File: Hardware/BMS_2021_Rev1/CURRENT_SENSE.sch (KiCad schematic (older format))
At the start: 5 parts

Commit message: cell filter mods, changing current sense circuit, 3v3/5v worked on
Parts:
- removed R?: R_Shunt, symbol Device:R_Shunt
- added R? (x3): 5mΩ, symbol Device:R
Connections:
- wire segments 38 -> 39
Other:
- note removed: "Doucmentation says connect VBUS to power supply rail, does this work\n"
- note removed: "Where should PV and ground go?\n"
- moved on the sheet: C?, R?

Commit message: changed current sense circuit to op amp
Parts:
- removed C?: C, symbol Device:C
- removed R? (x2): R, symbol Device:R
- removed U?: INA226, Package_SO:VSSOP-10_3x3mm_P0.5mm, symbol Analog_ADC:INA226
- added Q?: Q_NMOS_DGS, symbol Device:Q_NMOS_DGS
- added R? (x2): 27Ω, symbol Device:R
- added R?: 300Ω, symbol Device:R
- added U?: OPAMP, symbol pspice:OPAMP
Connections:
- net labels removed: +5V, I2C_Interface(?)
- wire segments 39 -> 24
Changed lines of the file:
@@
 	1950 850  2050 850
-Wire Wire Line
-	1550 1100 1550 850
 Wire Wire Line
 	1550 850  1650 850
@@
 	0    1    1    0
 $EndComp
-Connection ~ 6450 2900
+$Comp
+L pspice:OPAMP U?
+U 1 1 5F835DEC
+P 2200 1700
+F 0 "U?" V 2154 2044 50  0000 L CNN
+F 1 "OPAMP" V 2245 2044 50  0000 L CNN
+F 2 "" H 2200 1700 50  0001 C CNN
+F 3 "~" H 2200 1700 50  0001 C CNN
+	1    2200 1700
+	0    1    1    0
+$EndComp
+$Comp
+L Device:R R?
+U 1 1 5F8362F1
+P 1850 1150
+F 0 "R?" V 1760 1150 50  0000 C CNN
+F 1 "27Ω" V 1850 1150 39  0000 C CNN
+F 2 "" V 1780 1150 50  0001 C CNN
+F 3 "~" H 1850 1150 50  0001 C CNN
+	1    1850 1150
+	0    1    1    0
+$EndComp
+$Comp
+L Device:R R?
+U 1 1 5F83721F
+P 2550 1150
+F 0 "R?" V 2460 1150 50  0000 C CNN
+F 1 "27Ω" V 2550 1150 39  0000 C CNN
+F 2 "" V 2480 1150 50  0001 C CNN
+F 3 "~" H 2550 1150 50  0001 C CNN
+	1    2550 1150
+	0    1    1    0
+$EndComp
 Wire Wire Line
-	6450 3050 6450 2900
+	2700 1150 2850 1150
 Wire Wire Line
-	7100 1650 7100 3050
-Text GLabel 6650 2350 3    50   Output ~ 0
-I2C_Interface(?)
-Text GLabel 6200 2350 0    50   Output ~ 0
-I2C_Interface(?)
+	1550 1150 1700 1150
+Wire Wire Line
+	1550 850  1550 1150
+Wire Wire Line
+	2000 1150 2100 1150
+Wire Wire Line
+	2300 1150 2400 1150
+Wire Wire Line
+	1900 1600 1800 1600
+Wire Wire Line
+	1800 1600 1800 1650
+Wire Wire Line
+	2500 1600 2700 1600
+Text HLabel 2700 1600 2    50   Input ~ 0
+PV
 $Comp
 L power:GND #PWR?
-U 1 1 5F7FBB9B
-P 7200 2050
-AR Path="/5F80E1AD/5F7FBB9B" Ref="#PWR?"  Part="1"
-AR Path="/5F80341F/5F7FBB9B" Ref="#PWR?"  Part="1"
-F 0 "#PWR?" H 7200 1800 50  0001 C CNN
-F 1 "GND" H 7205 1877 50  0000 C CNN
-F 2 "" H 7200 2050 50  0001 C CNN
-F 3 "" H 7200 2050 50  0001 C CNN
-	1    7200 2050
-	1    0    0    -1
-$EndComp
-$Comp
-L Device:C C?
-U 1 1 5F7FB581
-P 7200 1900
-AR Path="/5F80E1AD/5F7FB581" Ref="C?"  Part="1"
-AR Path="/5F80341F/5F7FB581" Ref="C?"  Part="1"
-F 0 "C?" H 7315 1946 50  0000 L CNN
-F 1 "C" H 7315 1855 50  0000 L CNN
-F 2 "" H 7238 1750 50  0001 C CNN
-F 3 "~" H 7200 1900 50  0001 C CNN
-	1    7200 1900
+U 1 1 5F83E3C7
+P 1800 1650
+F 0 "#PWR?" H 1800 1400 50  0001 C CNN
+F 1 "GND" H 1805 1477 50  0000 C CNN
+F 2 "" H 1800 1650 50  0001 C CNN
+F 3 "" H 1800 1650 50  0001 C CNN
+	1    1800 1650
 	1    0    0    -1
 $EndComp
 Wire Wire Line
-	7100 1650 7100 1550
-Connection ~ 7100 1650
+	2850 850  2850 1150
 Wire Wire Line
-	7200 1650 7200 1750
+	2100 1150 2100 1300
 Wire Wire Line
-	7100 1650 7200 1650
-Connection ~ 7100 1550
+	2300 1150 2300 1400
+Connection ~ 2100 1300
 Wire Wire Line
-	6450 3050 7100 3050
+	2100 1300 2100 1400
 Wire Wire Line
-	6450 2900 6450 2750
+	1550 1300 1550 2300
 Wire Wire Line
-	6300 2900 6450 2900
-Wire Wire Line
-	6300 2750 6300 2900
-Wire Wire Line
-	6500 2300 6500 2400
-Connection ~ 6500 2300
-Wire Wire Line
-	6650 2300 6650 2350
-Wire Wire Line
-	6500 2300 6650 2300
-Wire Wire Line
-	6300 2350 6300 2450
-Connection ~ 6300 2350
-Wire Wire Line
-	6300 2350 6200 2350
-Wire Wire Line
-	6400 1950 6400 2150
-Wire Wire Line
-	6300 2150 6300 2350
-Wire Wire Line
-	6400 2150 6300 2150
-Wire Wire Line
-	6450 2400 6450 2450
-Wire Wire Line
-	6500 2400 6450 2400
-Wire Wire Line
-	6500 1950 6500 2300
+	1550 1300 2100 1300
 $Comp
-L Device:R R?
-U 1 1 5F7F7183
-P 6450 2600
-AR Path="/5F80E1AD/5F7F7183" Ref="R?"  Part="1"
-AR Path="/5F80341F/5F7F7183" Ref="R?"  Part="1"
-F 0 "R?" H 6520 2646 50  0000 L CNN
-F 1 "R" H 6520 2555 50  0000 L CNN
-F 2 "" V 6380 2600 50  0001 C CNN
-F 3 "~" H 6450 2600 50  0001 C CNN
-	1    6450 2600
-	1    0    0    -1
-$EndComp
-$Comp
-L Device:R R?
-U 1 1 5F7F6224
-P 6300 2600
-AR Path="/5F80E1AD/5F7F6224" Ref="R?"  Part="1"
-AR Path="/5F80341F/5F7F6224" Ref="R?"  Part="1"
-F 0 "R?" H 6150 2650 50  0000 L CNN
-F 1 "R" H 6150 2550 50  0000 L CNN
-F 2 "" V 6230 2600 50  0001 C CNN
-F 3 "~" H 6300 2600 50  0001 C CNN
-	1    6300 2600
+L Device:Q_NMOS_DGS Q?
+U 1 1 5F852FE1
+P 2100 2300
+F 0 "Q?" H 2304 2346 50  0000 L CNN
+F 1 "Q_NMOS_DGS" H 2304 2255 50  0000 L CNN
+F 2 "" H 2300 2400 50  0001 C CNN
+F 3 "~" H 2100 2300 50  0001 C CNN
+	1    2100 2300
 	1    0    0    -1
 $EndComp
 Wire Wire Line
-	6800 1150 6800 1000
+	2200 2000 2200 2100
+Wire Wire Line
+	1550 2300 1900 2300
+Wire Wire Line
+	2200 2500 2200 2750
+$Comp
+L Device:R R?
+U 1 1 5F85658D
+P 2200 2900
+F 0 "R?" H 2130 2900 50  0000 R CNN
+F 1 "300Ω" V 2200 2980 39  0000 R CNN
+F 2 "" V 2130 2900 50  0001 C CNN
+F 3 "~" H 2200 2900 50  0001 C CNN
+	1    2200 2900
+	-1   0    0    1
+$EndComp
+Wire Wire Line
+	2200 3050 2200 3150
 $Comp
 L power:GND #PWR?
-U 1 1 5F7F4F0A
-P 6800 2150
-AR Path="/5F80E1AD/5F7F4F0A" Ref="#PWR?"  Part="1"
-AR Path="/5F80341F/5F7F4F0A" Ref="#PWR?"  Part="1"
-F 0 "#PWR?" H 6800 1900 50  0001 C CNN
-F 1 "GND" H 6805 1977 50  0000 C CNN
-F 2 "" H 6800 2150 50  0001 C CNN
-F 3 "" H 6800 2150 50  0001 C CNN
-	1    6800 2150
+U 1 1 5F859B0F
+P 2200 3150
+F 0 "#PWR?" H 2200 2900 50  0001 C CNN
+F 1 "GND" H 2205 2977 50  0000 C CNN
+F 2 "" H 2200 3150 50  0001 C CNN
+F 3 "" H 2200 3150 50  0001 C CNN
+	1    2200 3150
 	1    0    0    -1
 $EndComp
-Connection ~ 6800 2050
-Wire Wire Line
-	6800 2050 6800 2150
-Wire Wire Line
-	6800 2050 6800 1950
-Wire Wire Line
-	6700 2050 6800 2050
-Wire Wire Line
-	6700 1950 6700 2050
-Wire Wire Line
-	6300 1150 6300 1000
-Wire Wire Line
-	6400 1150 6400 1000
-Wire Wire Line
-	5900 1550 6000 1550
-Wire Wire Line
-	5900 1650 5900 1550
-Wire Wire Line
-	7100 1550 7100 1450
-Wire Wire Line
-	7000 1550 7100 1550
-$Comp
-L Analog_ADC:INA226 U?
-U 1 1 5F80EB78
-P 6500 1550
-AR Path="/5F80E1AD/5F80EB78" Ref="U?"  Part="1"
-AR Path="/5F80341F/5F80EB78" Ref="U?"  Part="1"
-F 0 "U?" V 6250 950 50  0000 C CNN
-F 1 "INA226" V 6350 950 50  0000 C CNN
-F 2 "Package_SO:VSSOP-10_3x3mm_P0.5mm" H 7300 1100 50  0001 C CNN
-F 3 "http://www.ti.com/lit/ds/symlink/ina226.pdf" H 6850 1450 50  0001 C CNN
-	1    6500 1550
-	0    1    1    0
-$EndComp
-$Comp
-L power:+5V #PWR?
-U 1 1 5F810654
-P 7100 1450
-AR Path="/5F80E1AD/5F810654" Ref="#PWR?"  Part="1"
-AR Path="/5F80341F/5F810654" Ref="#PWR?"  Part="1"
-F 0 "#PWR?" H 7100 1300 50  0001 C CNN
-F 1 "+5V" H 7115 1623 50  0000 C CNN
-F 2 "" H 7100 1450 50  0001 C CNN
-F 3 "" H 7100 1450 50  0001 C CNN
-	1    7100 1450
-	1    0    0    -1
-$EndComp
-$Comp
-L power:GND #PWR?
-U 1 1 5F80FF68
-P 5900 1650
-AR Path="/5F80E1AD/5F80FF68" Ref="#PWR?"  Part="1"
-AR Path="/5F80341F/5F80FF68" Ref="#PWR?"  Part="1"
-F 0 "#PWR?" H 5900 1400 50  0001 C CNN
-F 1 "GND" H 5905 1477 50  0000 C CNN
-F 2 "" H 5900 1650 50  0001 C CNN
-F 3 "" H 5900 1650 50  0001 C CNN
-	1    5900 1650
-	1    0    0    -1
-$EndComp
-Wire Wire Line
-	2850 850  2850 1050
 $EndSCHEMATC

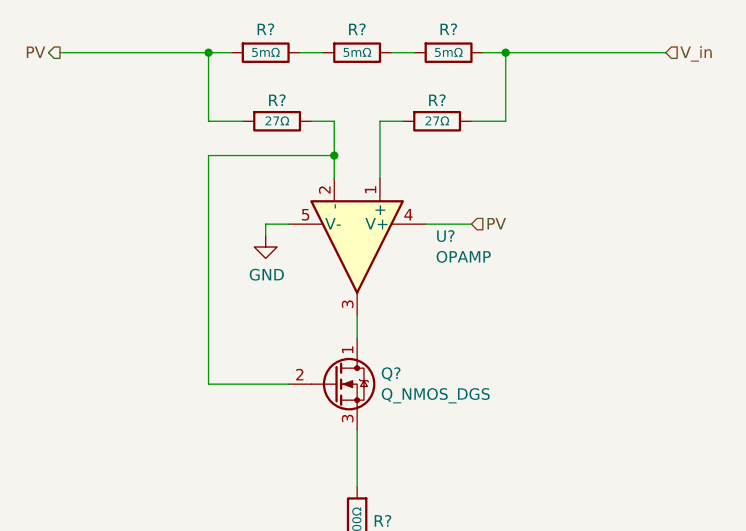
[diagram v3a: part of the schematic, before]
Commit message: buzzer started, 5v buck needs R values
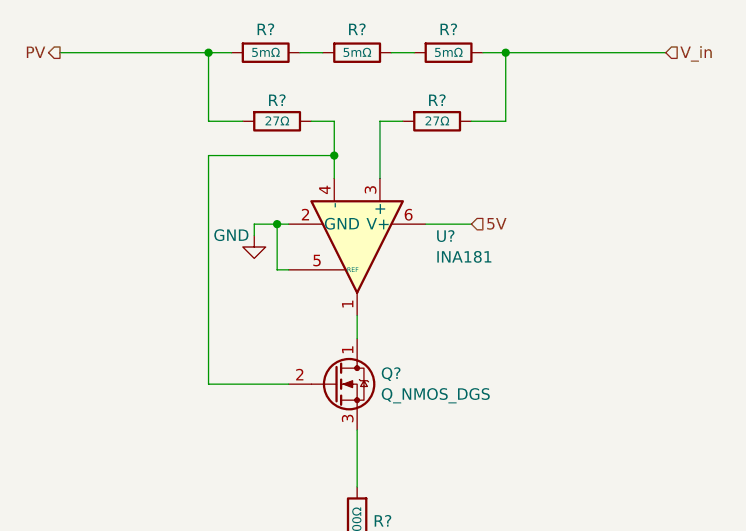
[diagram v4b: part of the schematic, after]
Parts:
- removed U?: OPAMP, symbol pspice:OPAMP
- added U?: INA181, Package_TO_SOT_SMD:SOT-23-6, symbol Amplifier_Current:INA181
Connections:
- net GND: now also U?.2 (GND), U?.5 (REF)
- net at R?.2: now also U?.3 (+)
- net at Q?.2 (G), R?.1: now also U?.4 (-)
- net at Q?.1 (D): now also U?.1
- new net 5V: U?.6 (V+)
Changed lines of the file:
@@
 EELAYER 30 0
 EELAYER END
-$Descr A4 11693 8268
+$Descr A 11000 8500
 encoding utf-8
 Sheet 3 10
@@
 	2300 1150 2400 1150
 Wire Wire Line
-	1900 1600 1800 1600
-Wire Wire Line
-	1800 1600 1800 1650
-Wire Wire Line
 	2500 1600 2700 1600
 Text HLabel 2700 1600 2    50   Input ~ 0
-PV
+5V
 $Comp
 L power:GND #PWR?
 U 1 1 5F83E3C7
-P 1800 1650
-F 0 "#PWR?" H 1800 1400 50  0001 C CNN
-F 1 "GND" H 1805 1477 50  0000 C CNN
-F 2 "" H 1800 1650 50  0001 C CNN
-F 3 "" H 1800 1650 50  0001 C CNN
-	1    1800 1650
+P 1750 1650
+F 0 "#PWR?" H 1750 1400 50  0001 C CNN
+F 1 "GND" H 1650 1650 50  0000 C CNN
+F 2 "" H 1750 1650 50  0001 C CNN
+F 3 "" H 1750 1650 50  0001 C CNN
+	1    1750 1650
 	1    0    0    -1
 $EndComp
@@
 $EndComp
 $Comp
-L pspice:OPAMP U?
-U 1 1 5F835DEC
+L Amplifier_Current:INA181 U?
+U 1 1 5F85CDFE
 P 2200 1700
 F 0 "U?" V 2154 2044 50  0000 L CNN
-F 1 "OPAMP" V 2245 2044 50  0000 L CNN
-F 2 "" H 2200 1700 50  0001 C CNN
-F 3 "~" H 2200 1700 50  0001 C CNN
+F 1 "INA181" V 2245 2044 50  0000 L CNN
+F 2 "Package_TO_SOT_SMD:SOT-23-6" H 2250 1750 50  0001 C CNN
+F 3 "http://www.ti.com/lit/ds/symlink/ina181.pdf" H 2350 1850 50  0001 C CNN
 	1    2200 1700
 	0    1    1    0
 $EndComp
+Wire Wire Line
+	1900 1600 1850 1600
+Wire Wire Line
+	1750 1600 1750 1650
+Wire Wire Line
+	1900 1800 1850 1800
+Wire Wire Line
+	1850 1800 1850 1600
+Connection ~ 1850 1600
+Wire Wire Line
+	1750 1600 1850 1600
 $EndSCHEMATC

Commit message: changed ICs
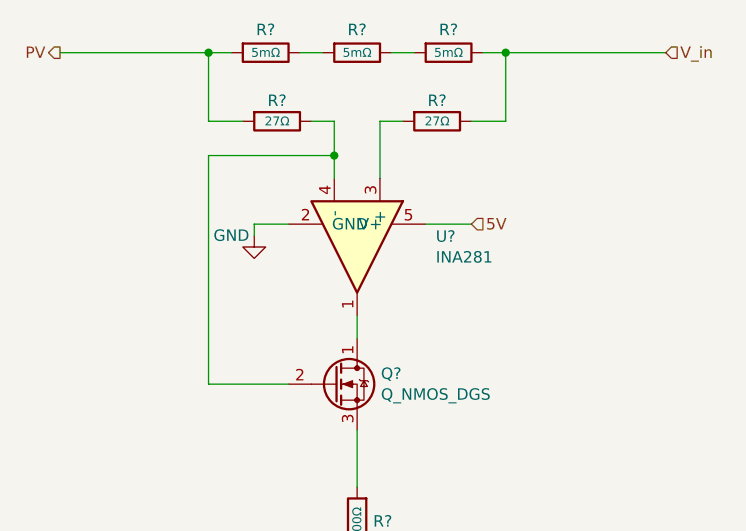
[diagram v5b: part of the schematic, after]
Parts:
- removed U?: INA181, Package_TO_SOT_SMD:SOT-23-6, symbol Amplifier_Current:INA181
- added U?: INA281, symbol MRDT_ICs:INA281
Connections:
- net 5V: now also U?.5 (V+)
- net GND: now also U?.2 (GND)
- net at Q?.2 (G), R?.1: now also U?.4 (-)
- net at R?.2: now also U?.3 (+)
- net at Q?.1 (D): now also U?.1
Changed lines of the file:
@@
 	1    0    0    -1
 $EndComp
+Wire Wire Line
+	1750 1600 1750 1650
 $Comp
-L Amplifier_Current:INA181 U?
-U 1 1 5F85CDFE
-P 2200 1700
-F 0 "U?" V 2154 2044 50  0000 L CNN
-F 1 "INA181" V 2245 2044 50  0000 L CNN
-F 2 "Package_TO_SOT_SMD:SOT-23-6" H 2250 1750 50  0001 C CNN
-F 3 "http://www.ti.com/lit/ds/symlink/ina181.pdf" H 2350 1850 50  0001 C CNN
-	1    2200 1700
+L MRDT_ICs:INA281 U?
+U 1 1 5F86B7DF
+P 2200 1600
+F 0 "U?" V 2254 1944 50  0000 L CNN
+F 1 "INA281" V 2345 1944 50  0000 L CNN
+F 2 "" H 2450 1800 50  0001 C CNN
+F 3 "" H 2450 1800 50  0001 C CNN
+	1    2200 1600
 	0    1    1    0
 $EndComp
 Wire Wire Line
-	1900 1600 1850 1600
-Wire Wire Line
-	1750 1600 1750 1650
-Wire Wire Line
-	1900 1800 1850 1800
-Wire Wire Line
-	1850 1800 1850 1600
-Connection ~ 1850 1600
-Wire Wire Line
-	1750 1600 1850 1600
+	1750 1600 1900 1600
 $EndSCHEMATC

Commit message: idk what changed
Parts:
- R?: value 300Ω -> 330Ω
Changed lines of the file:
@@
 P 2200 2900
 F 0 "R?" H 2130 2900 50  0000 R CNN
-F 1 "300Ω" V 2200 2980 39  0000 R CNN
+F 1 "330Ω" V 2200 2980 39  0000 R CNN
 F 2 "" V 2130 2900 50  0001 C CNN
 F 3 "~" H 2200 2900 50  0001 C CNN
@@
 F 1 "INA281" V 2345 1944 50  0000 L CNN
 F 2 "" H 2450 1800 50  0001 C CNN
-F 3 "" H 2450 1800 50  0001 C CNN
+F 3 "https://www.ti.com/product/INA281" H 2450 1800 50  0001 C CNN
 	1    2200 1600
 	0    1    1    0

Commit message: done (need to do LEDs)
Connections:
- net pack_i_sense: now reaches Q?.3 (S), R?.2
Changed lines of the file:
@@
 $Descr A 11000 8500
 encoding utf-8
-Sheet 3 10
+Sheet 3 11
 Title ""
 Date ""
@@
 	1550 2300 1900 2300
 Wire Wire Line
-	2200 2500 2200 2750
+	2200 2500 2200 2650
 $Comp
 L Device:R R?
@@
 Wire Wire Line
 	1750 1600 1900 1600
+Wire Wire Line
+	2200 2650 2525 2650
+Connection ~ 2200 2650
+Wire Wire Line
+	2200 2650 2200 2750
+Text HLabel 2525 2650 2    50   Output ~ 0
+pack_i_sense
 $EndSCHEMATC

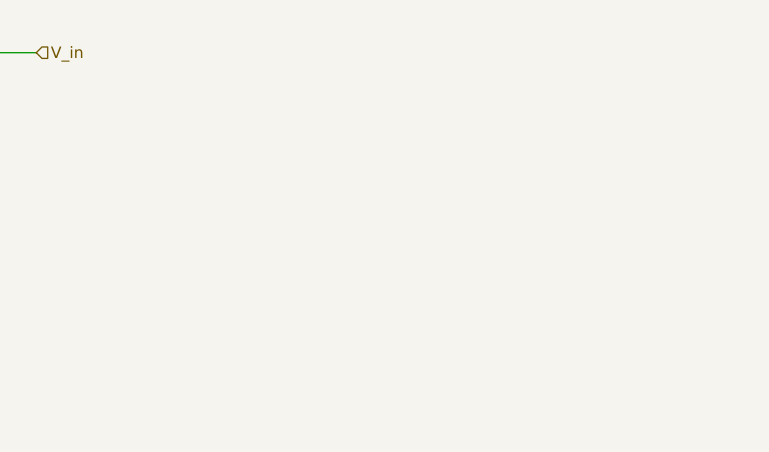
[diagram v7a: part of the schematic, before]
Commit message: notes from PDR made. to be fixed
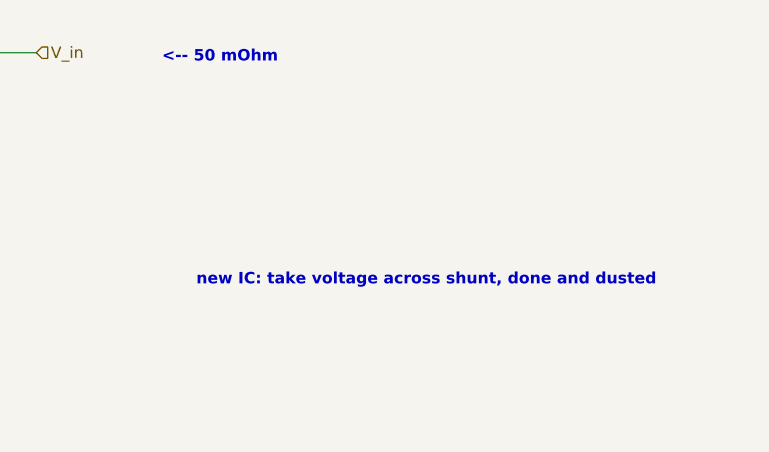
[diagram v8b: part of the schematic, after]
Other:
- note added: "<-- 50 mOhm\n"
- note added: "new IC: take voltage across shunt, done and dusted\n"
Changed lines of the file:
@@
 Text HLabel 2525 2650 2    50   Output ~ 0
 pack_i_sense
+Text Notes 4100 900  0    50   ~ 10
+<-- 50 mOhm\n
+Text Notes 4250 1875 0    50   ~ 10
+new IC: take voltage across shunt, done and dusted\n
 $EndSCHEMATC
